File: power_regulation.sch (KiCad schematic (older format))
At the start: 6 parts

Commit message: added pullups/downs as necessary, added test pts
also added interrupt conn to msp from charger, made led part for generic
indicators, added generic indicators to psu's
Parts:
- removed D?: LED, ~, symbol LED
- added D?: LED_GENERIC_SMD, ~, symbol LED_GENERIC_SMD
- R?: value 500/1k -> 700
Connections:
- net labels added: PWR_EN
- wire segments 33 -> 25
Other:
- note added: "1.9V @ 2mA"
- note added: "Indicator LED"
- note removed: "3.3V Indicator LED"
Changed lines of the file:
@@
 $Descr A4 11693 8268
 encoding utf-8
-Sheet 17 18
+Sheet 15 18
 Title ""
-Date "14 dec 2013"
+Date "18 dec 2013"
 Rev ""
 Comp ""
@@
 P 4150 1950
 F 0 "R?" V 4230 1950 40  0000 C CNN
-F 1 "500/1k" V 4157 1951 40  0000 C CNN
+F 1 "700" V 4157 1951 40  0000 C CNN
 F 2 "~" V 4080 1950 30  0000 C CNN
 F 3 "~" H 4150 1950 30  0000 C CNN
 	1    4150 1950
 	-1   0    0    1
-$EndComp
-$Comp
-L LED D?
-U 1 1 522573BB
-P 4150 2450
-F 0 "D?" H 4150 2550 50  0000 C CNN
-F 1 "LED" H 4150 2350 50  0000 C CNN
-F 2 "~" H 4150 2450 60  0000 C CNN
-F 3 "~" H 4150 2450 60  0000 C CNN
-	1    4150 2450
-	0    1    1    0
 $EndComp
 $Comp
@@
 $EndComp
 Wire Wire Line
-	1350 850  1450 850
-Wire Wire Line
-	1450 850  2100 850
-Wire Wire Line
-	2100 850  2300 850
+	1350 850  2300 850
 Wire Wire Line
 	2100 2850 2100 2900
 Wire Wire Line
-	2100 2900 2200 2900
-Wire Wire Line
-	2200 2900 2300 2900
-Wire Wire Line
-	2200 2850 2200 2900
-Wire Wire Line
-	2200 2900 2200 3050
+	2100 2900 2300 2900
+Wire Wire Line
+	2200 2850 2200 3050
 Connection ~ 2200 2900
 Wire Wire Line
@@
 	1400 2300 1400 2350
 Wire Wire Line
-	3800 2100 3800 2650
-Wire Wire Line
-	3800 2650 3800 2700
+	3800 2100 3800 2700
 Wire Wire Line
 	2950 1800 3050 1800
@@
 	1450 1450 1450 1350
 Connection ~ 1450 850
-Wire Wire Line
-	4150 2200 4150 2250
 Text HLabel 4250 1700 2    60   Output ~ 0
 3.3V_600mA
-Text Notes 4450 2650 1    60   ~ 0
-3.3V Indicator LED
+Text Notes 4950 2500 2    60   ~ 0
+Indicator LED
 Text HLabel 1350 850  0    60   Input ~ 0
 BATT_IN
@@
 	1    0    0    -1
 $EndComp
-Text HLabel 1350 2200 0    60   Input ~ 0
-BATT_IN
 Wire Wire Line
 	1050 2050 1450 2050
@@
 Connection ~ 3800 1700
 Wire Wire Line
-	2950 1700 3050 1700
-Wire Wire Line
-	3050 1700 3800 1700
-Wire Wire Line
-	3800 1700 4150 1700
-Wire Wire Line
-	4150 1700 4250 1700
+	2950 1700 4250 1700
 Connection ~ 4150 1700
+Text HLabel 1350 2200 0    60   Input ~ 0
+PWR_EN
+$Comp
+L LED_GENERIC_SMD D?
+U 1 1 52B2DEF7
+P 4150 2450
+F 0 "D?" H 4150 2550 50  0000 C CNN
+F 1 "LED_GENERIC_SMD" H 4150 2300 50  0001 C CNN
+F 2 "~" H 4150 2450 60  0000 C CNN
+F 3 "~" H 4150 2450 60  0000 C CNN
+	1    4150 2450
+	0    1    1    0
+$EndComp
+Wire Wire Line
+	4150 2200 4150 2250
+Text Notes 4350 2600 0    60   ~ 0
+1.9V @ 2mA
 $EndSCHEMATC

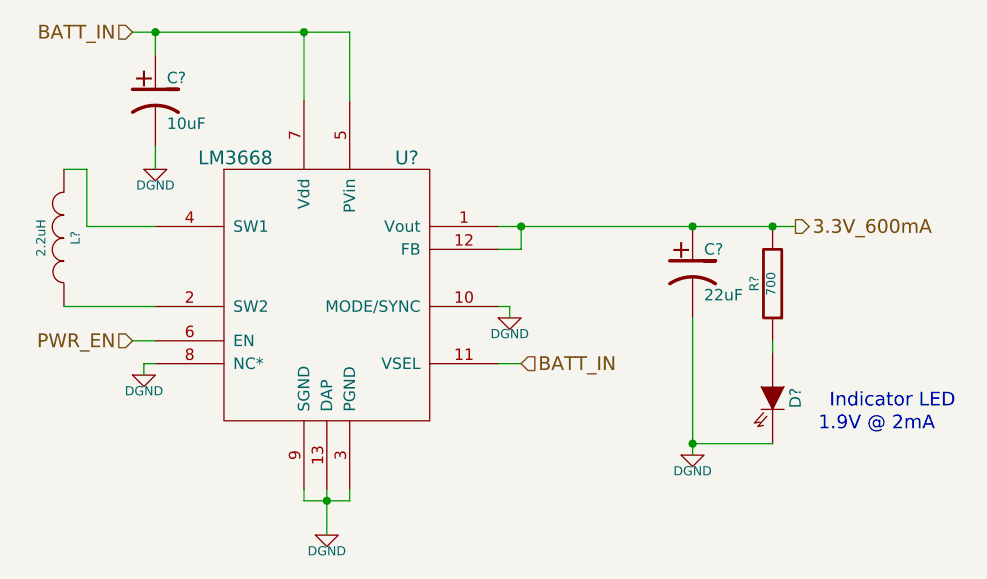
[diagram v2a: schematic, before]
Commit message: various fixes due to issues found in ERC
learned how to use invisible pins
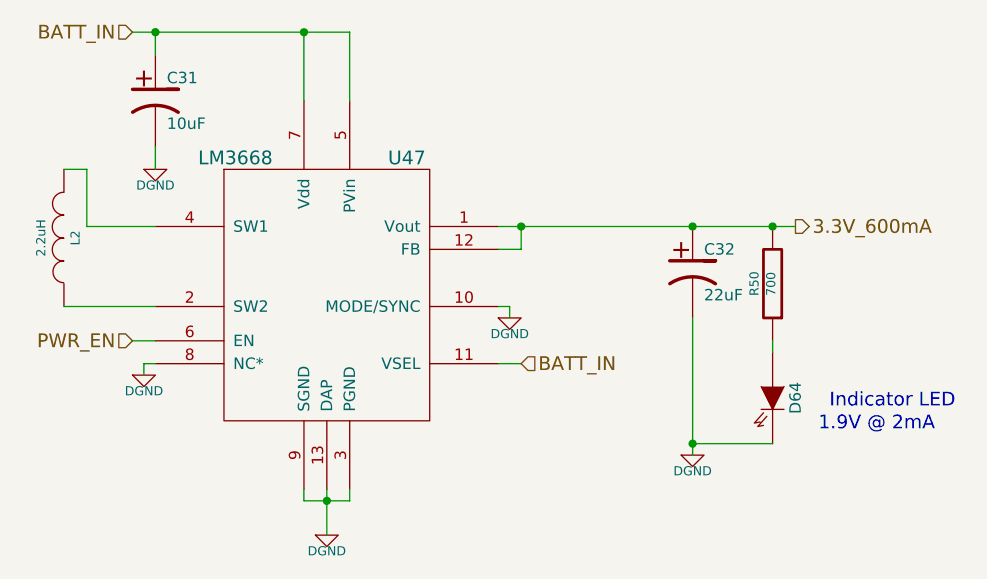
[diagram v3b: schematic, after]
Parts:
- gave numbers to parts that had none: 6
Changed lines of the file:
@@
 Sheet 15 18
 Title ""
-Date "18 dec 2013"
+Date "20 dec 2013"
 Rev ""
 Comp ""
@@
 $EndDescr
 $Comp
-L R R?
+L R R50
 U 1 1 5225739D
 P 4150 1950
-F 0 "R?" V 4230 1950 40  0000 C CNN
+F 0 "R50" V 4230 1950 40  0000 C CNN
 F 1 "700" V 4157 1951 40  0000 C CNN
 F 2 "~" V 4080 1950 30  0000 C CNN
@@
 $EndComp
 $Comp
-L LM3668 U?
+L LM3668 U47
 U 1 1 529A2E0E
 P 2200 2000
-F 0 "U?" H 2550 2600 60  0000 C CNN
+F 0 "U47" H 2550 2600 60  0000 C CNN
 F 1 "LM3668" H 1800 2600 60  0000 C CNN
 F 2 "" H 2200 1950 60  0000 C CNN
@@
 $EndComp
 $Comp
-L CP1 C?
+L CP1 C31
 U 1 1 529A2E1F
 P 1450 1150
-F 0 "C?" H 1500 1250 50  0000 L CNN
+F 0 "C31" H 1500 1250 50  0000 L CNN
 F 1 "10uF" H 1500 1050 50  0000 L CNN
 F 2 "~" H 1450 1150 60  0000 C CNN
@@
 $EndComp
 $Comp
-L INDUCTOR L?
+L INDUCTOR L2
 U 1 1 529A2E2E
 P 1050 1750
-F 0 "L?" V 1000 1750 40  0000 C CNN
+F 0 "L2" V 1000 1750 40  0000 C CNN
 F 1 "2.2uH" V 1150 1750 40  0000 C CNN
 F 2 "~" H 1050 1750 60  0000 C CNN
@@
 $EndComp
 $Comp
-L CP1 C?
+L CP1 C32
 U 1 1 529A2E3D
 P 3800 1900
-F 0 "C?" H 3850 2000 50  0000 L CNN
+F 0 "C32" H 3850 2000 50  0000 L CNN
 F 1 "22uF" H 3850 1800 50  0000 L CNN
 F 2 "~" H 3800 1900 60  0000 C CNN
@@
 Connection ~ 2100 850
 $Comp
-L DGND #PWR?
+L DGND #PWR0104
 U 1 1 52A4E648
 P 1400 2350
-F 0 "#PWR?" H 1400 2350 40  0001 C CNN
+F 0 "#PWR0104" H 1400 2350 40  0001 C CNN
 F 1 "DGND" H 1400 2280 40  0000 C CNN
 F 2 "" H 1400 2350 60  0000 C CNN
@@
 $EndComp
 $Comp
-L DGND #PWR?
+L DGND #PWR0105
 U 1 1 52A4E64E
 P 2200 3050
-F 0 "#PWR?" H 2200 3050 40  0001 C CNN
+F 0 "#PWR0105" H 2200 3050 40  0001 C CNN
 F 1 "DGND" H 2200 2980 40  0000 C CNN
 F 2 "" H 2200 3050 60  0000 C CNN
@@
 $EndComp
 $Comp
-L DGND #PWR?
+L DGND #PWR0106
 U 1 1 52A4E654
 P 3000 2100
-F 0 "#PWR?" H 3000 2100 40  0001 C CNN
+F 0 "#PWR0106" H 3000 2100 40  0001 C CNN
 F 1 "DGND" H 3000 2030 40  0000 C CNN
 F 2 "" H 3000 2100 60  0000 C CNN
@@
 $EndComp
 $Comp
-L DGND #PWR?
+L DGND #PWR0107
 U 1 1 52A4E65A
 P 3800 2700
-F 0 "#PWR?" H 3800 2700 40  0001 C CNN
+F 0 "#PWR0107" H 3800 2700 40  0001 C CNN
 F 1 "DGND" H 3800 2630 40  0000 C CNN
 F 2 "" H 3800 2700 60  0000 C CNN
@@
 	1150 1450 1050 1450
 $Comp
-L DGND #PWR?
+L DGND #PWR0108
 U 1 1 52A4E6EF
 P 1450 1450
-F 0 "#PWR?" H 1450 1450 40  0001 C CNN
+F 0 "#PWR0108" H 1450 1450 40  0001 C CNN
 F 1 "DGND" H 1450 1380 40  0000 C CNN
 F 2 "" H 1450 1450 60  0000 C CNN
@@
 PWR_EN
 $Comp
-L LED_GENERIC_SMD D?
+L LED_GENERIC_SMD D64
 U 1 1 52B2DEF7
 P 4150 2450
-F 0 "D?" H 4150 2550 50  0000 C CNN
+F 0 "D64" H 4150 2550 50  0000 C CNN
 F 1 "LED_GENERIC_SMD" H 4150 2300 50  0001 C CNN
 F 2 "~" H 4150 2450 60  0000 C CNN

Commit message: placed components ... quite the task!
there is a lot of shit going on in this board... :D
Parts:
- renumbered C31 to C25, C32 to C26, D64 to D37, R50 to R45, U47 to U43
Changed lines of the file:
@@
 $Descr A4 11693 8268
 encoding utf-8
-Sheet 15 18
+Sheet 15 15
 Title ""
-Date "12 jan 2014"
+Date "18 jan 2014"
 Rev ""
 Comp ""
@@
 $EndDescr
 $Comp
-L R R50
+L R R45
 U 1 1 5225739D
 P 4150 1950
-F 0 "R50" V 4230 1950 40  0000 C CNN
+F 0 "R45" V 4230 1950 40  0000 C CNN
 F 1 "700" V 4157 1951 40  0000 C CNN
 F 2 "~" V 4080 1950 30  0000 C CNN
@@
 $EndComp
 $Comp
-L LM3668 U47
+L LM3668 U43
 U 1 1 529A2E0E
 P 2200 2000
-F 0 "U47" H 2550 2600 60  0000 C CNN
+F 0 "U43" H 2550 2600 60  0000 C CNN
 F 1 "LM3668" H 1800 2600 60  0000 C CNN
 F 2 "" H 2200 1950 60  0000 C CNN
@@
 $EndComp
 $Comp
-L CP1 C31
+L CP1 C25
 U 1 1 529A2E1F
 P 1450 1150
-F 0 "C31" H 1500 1250 50  0000 L CNN
+F 0 "C25" H 1500 1250 50  0000 L CNN
 F 1 "10uF" H 1500 1050 50  0000 L CNN
 F 2 "~" H 1450 1150 60  0000 C CNN
@@
 $EndComp
 $Comp
-L CP1 C32
+L CP1 C26
 U 1 1 529A2E3D
 P 3800 1900
-F 0 "C32" H 3850 2000 50  0000 L CNN
+F 0 "C26" H 3850 2000 50  0000 L CNN
 F 1 "22uF" H 3850 1800 50  0000 L CNN
 F 2 "~" H 3800 1900 60  0000 C CNN
@@
 Connection ~ 2100 850
 $Comp
-L DGND #PWR0106
+L DGND #PWR092
 U 1 1 52A4E648
 P 1400 2350
-F 0 "#PWR0106" H 1400 2350 40  0001 C CNN
+F 0 "#PWR092" H 1400 2350 40  0001 C CNN
 F 1 "DGND" H 1400 2280 40  0000 C CNN
 F 2 "" H 1400 2350 60  0000 C CNN
@@
 $EndComp
 $Comp
-L DGND #PWR0107
+L DGND #PWR093
 U 1 1 52A4E64E
 P 2200 3050
-F 0 "#PWR0107" H 2200 3050 40  0001 C CNN
+F 0 "#PWR093" H 2200 3050 40  0001 C CNN
 F 1 "DGND" H 2200 2980 40  0000 C CNN
 F 2 "" H 2200 3050 60  0000 C CNN
@@
 $EndComp
 $Comp
-L DGND #PWR0108
+L DGND #PWR094
 U 1 1 52A4E654
 P 3000 2100
-F 0 "#PWR0108" H 3000 2100 40  0001 C CNN
+F 0 "#PWR094" H 3000 2100 40  0001 C CNN
 F 1 "DGND" H 3000 2030 40  0000 C CNN
 F 2 "" H 3000 2100 60  0000 C CNN
@@
 $EndComp
 $Comp
-L DGND #PWR0109
+L DGND #PWR095
 U 1 1 52A4E65A
 P 3800 2700
-F 0 "#PWR0109" H 3800 2700 40  0001 C CNN
+F 0 "#PWR095" H 3800 2700 40  0001 C CNN
 F 1 "DGND" H 3800 2630 40  0000 C CNN
 F 2 "" H 3800 2700 60  0000 C CNN
@@
 	1150 1450 1050 1450
 $Comp
-L DGND #PWR0110
+L DGND #PWR096
 U 1 1 52A4E6EF
 P 1450 1450
-F 0 "#PWR0110" H 1450 1450 40  0001 C CNN
+F 0 "#PWR096" H 1450 1450 40  0001 C CNN
 F 1 "DGND" H 1450 1380 40  0000 C CNN
 F 2 "" H 1450 1450 60  0000 C CNN
@@
 PWR_EN
 $Comp
-L LED_GENERIC_SMD D64
+L LED_GENERIC_SMD D37
 U 1 1 52B2DEF7
 P 4150 2450
-F 0 "D64" H 4150 2550 50  0000 C CNN
+F 0 "D37" H 4150 2550 50  0000 C CNN
 F 1 "LED_GENERIC_SMD" H 4150 2300 50  0001 C CNN
 F 2 "~" H 4150 2450 60  0000 C CNN
